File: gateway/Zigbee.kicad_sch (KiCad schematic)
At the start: 28 parts, among them IC1101 MIC5317-3.3xM5, IC1102 TXB0102DCT, IC1103 74LVC1G07, IC1104 74LVC1G07, M1101 RF-BM-2652

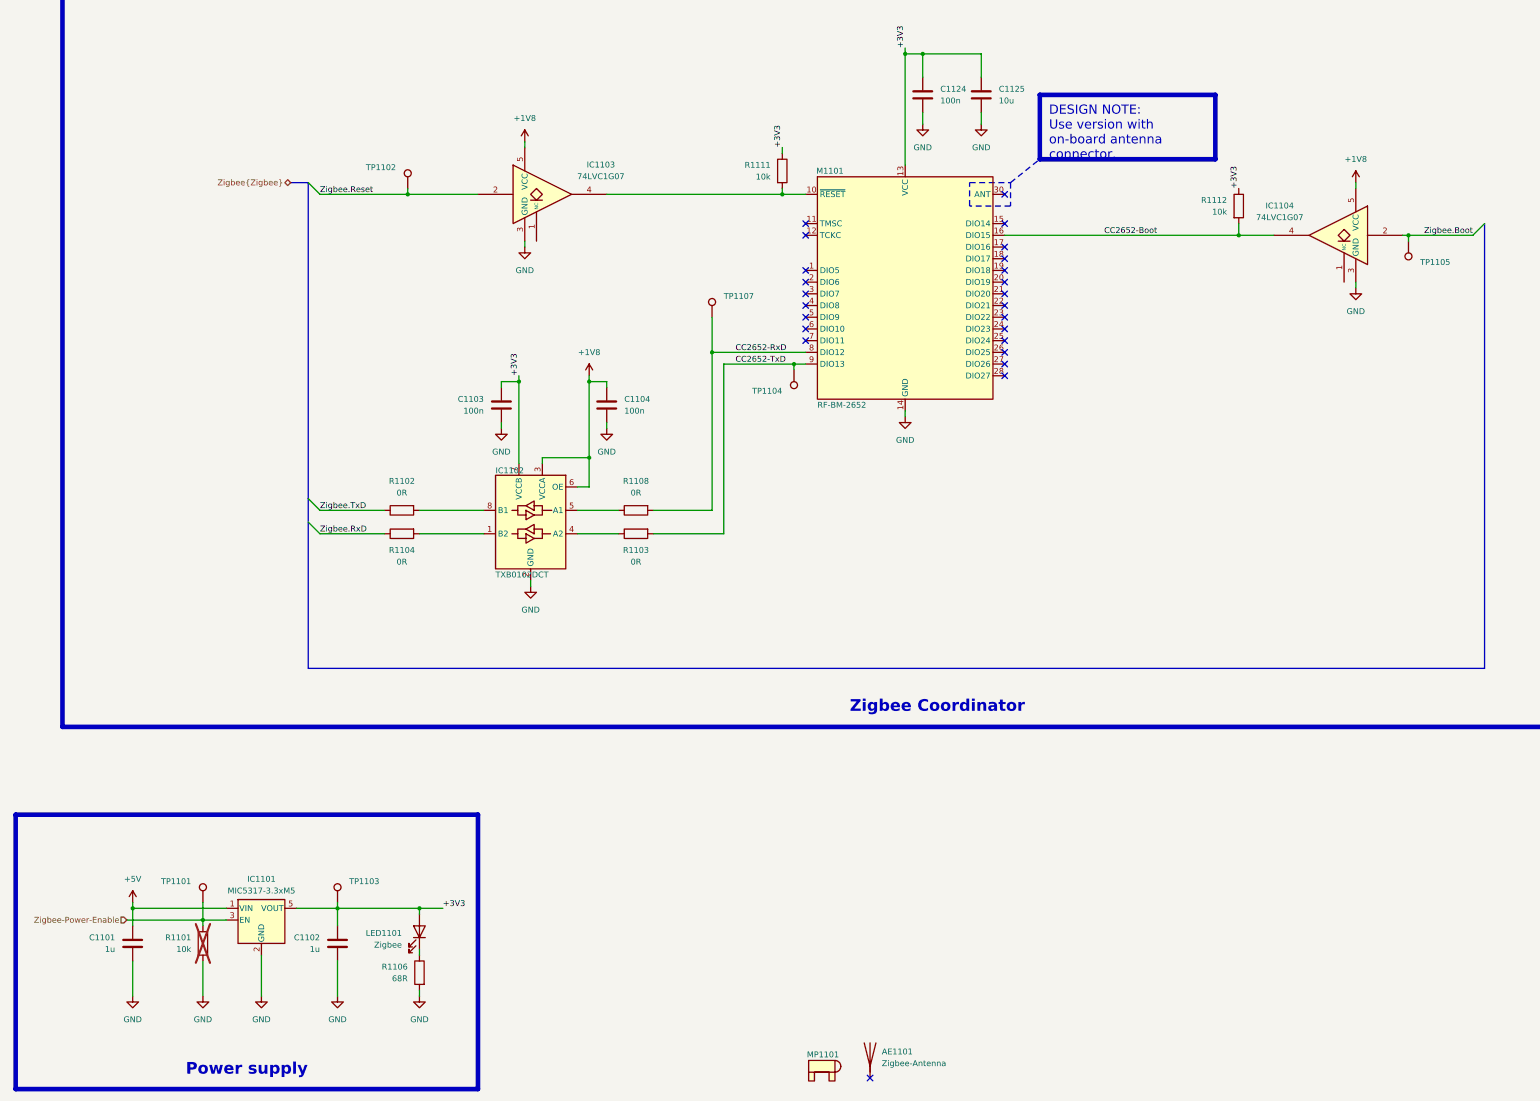
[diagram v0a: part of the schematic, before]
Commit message: Add INA219 for current measurement
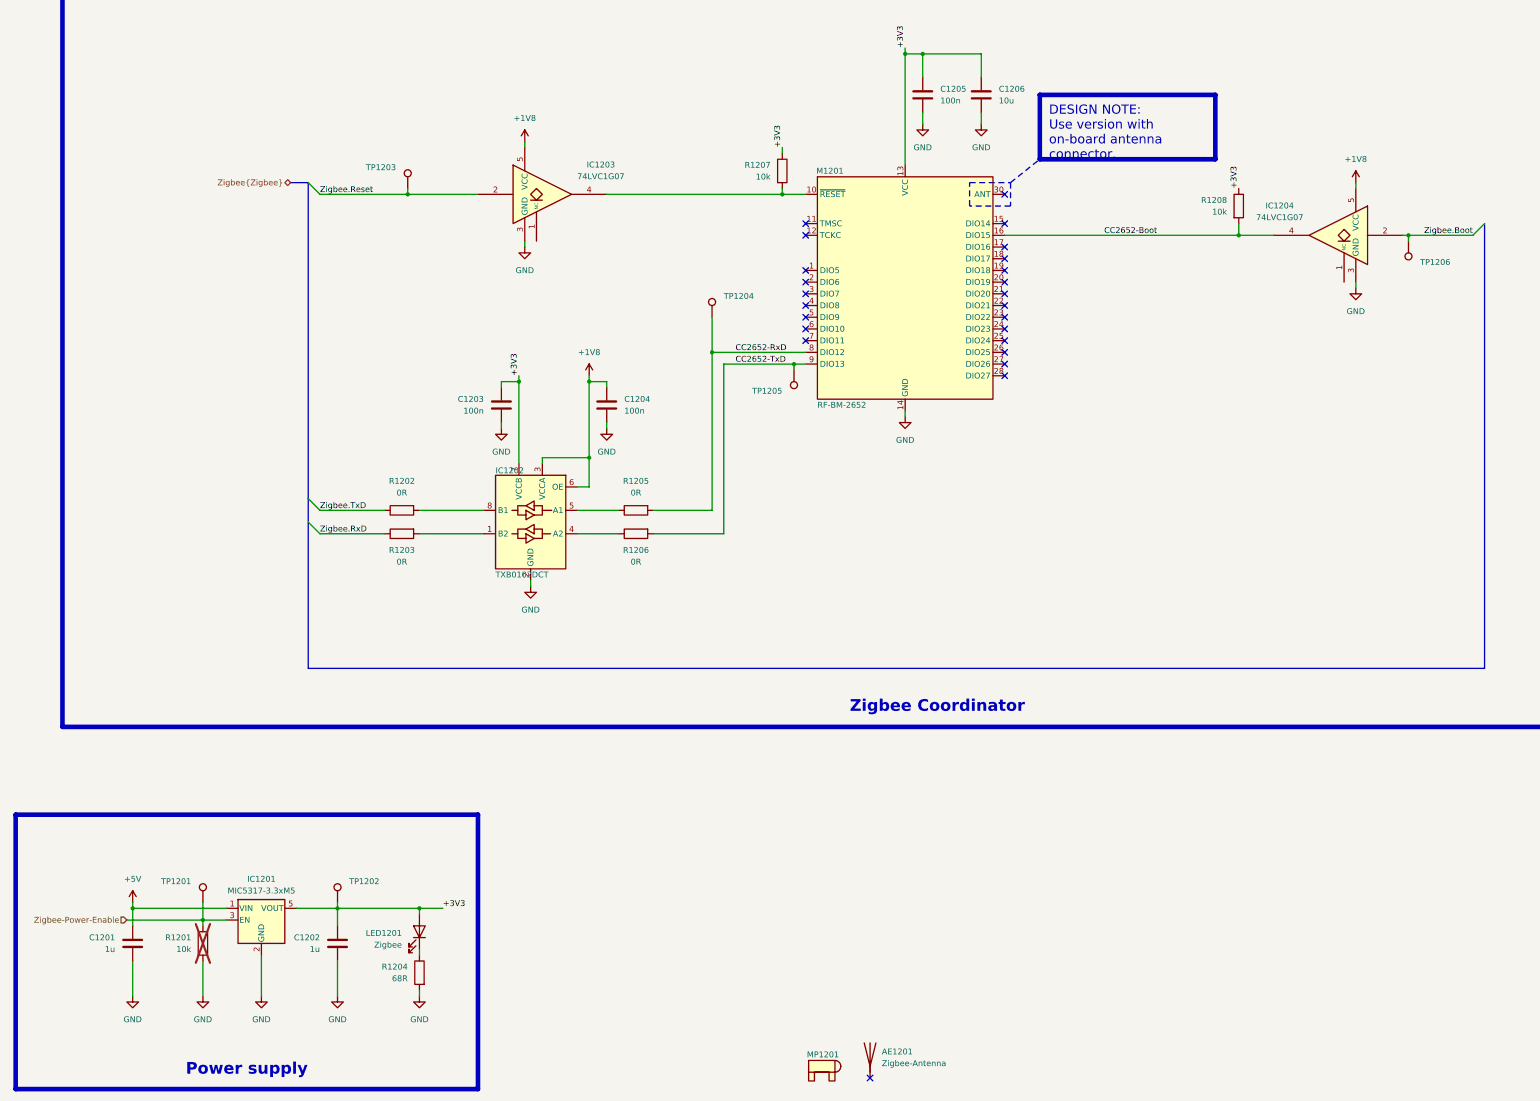
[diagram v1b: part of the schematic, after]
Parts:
- renumbered AE1101 to AE1201, C1101 to C1201, C1102 to C1202, C1103 to C1203, C1104 to C1204, C1124 to C1205, C1125 to C1206, IC1101 to IC1201, IC1102 to IC1202, IC1103 to IC1203, IC1104 to IC1204, LED1101 to LED1201, M1101 to M1201, MP1101 to MP1201, R1101 to R1201, R1102 to R1202, R1104 to R1203, R1106 to R1204, R1108 to R1205, R1103 to R1206, R1111 to R1207, R1112 to R1208, TP1101 to TP1201, TP1103 to TP1202, TP1102 to TP1203, TP1107 to TP1204, TP1104 to TP1205, TP1105 to TP1206

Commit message: Improving Thread
- Add boot signal for Thread MCU
- Add debug LED for nRF5340
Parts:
- TP1201, TP1202, TP1203, TP1204, TP1205, TP1206: value ~ -> (none)
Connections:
- net at IC1202.1 (B2): now also R1206.1; no longer R1203.2
- net at IC1202.4 (A2): now also R1203.2; no longer R1206.1
- net at IC1202.5 (A1): now also R1202.2; no longer R1205.1
- net at IC1202.8 (B1): now also R1205.1; no longer R1202.2
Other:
- moved on the sheet: C1203, C1204
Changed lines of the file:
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@@
 	)
 	(rectangle
-		(start 24.13 38.1)
-		(end 403.86 204.47)
+		(start 54.61 38.1)
+		(end 345.44 204.47)
 		(stroke
 			(width 1)
@@
 	(text_box "Zigbee Coordinator"
 		(exclude_from_sim no)
-		(at 25.4 194.31 0)
-		(size 377.19 8.89)
+		(at 55.88 194.31 0)
+		(size 288.29 8.89)
 		(margins 1.9049 1.9049 1.9049 1.9049)
 		(stroke
@@
 	)
 	(junction
-		(at 123.19 129.54)
+		(at 128.27 129.54)
 		(diameter 0)
 		(color 0 0 0 0)
@@
 	)
 	(junction
-		(at 138.43 146.05)
+		(at 113.03 146.05)
 		(diameter 0)
 		(color 0 0 0 0)
@@
 	)
 	(junction
-		(at 138.43 129.54)
+		(at 113.03 129.54)
 		(diameter 0)
 		(color 0 0 0 0)
@@
 	(wire
 		(pts
-			(xy 138.43 129.54) (xy 142.24 129.54)
+			(xy 113.03 129.54) (xy 109.22 129.54)
 		)
 		(stroke
@@
 	(wire
 		(pts
-			(xy 138.43 146.05) (xy 138.43 152.4)
+			(xy 113.03 146.05) (xy 113.03 152.4)
 		)
 		(stroke
@@
 	(wire
 		(pts
-			(xy 119.38 129.54) (xy 119.38 130.81)
+			(xy 132.08 129.54) (xy 132.08 130.81)
 		)
 		(stroke
@@
 	(wire
 		(pts
-			(xy 142.24 129.54) (xy 142.24 130.81)
+			(xy 109.22 129.54) (xy 109.22 130.81)
 		)
 		(stroke
@@
 	(wire
 		(pts
-			(xy 142.24 138.43) (xy 142.24 139.7)
+			(xy 109.22 138.43) (xy 109.22 139.7)
 		)
 		(stroke
@@
 	(wire
 		(pts
-			(xy 138.43 152.4) (xy 135.89 152.4)
+			(xy 113.03 152.4) (xy 115.57 152.4)
 		)
 		(stroke
@@
 	(wire
 		(pts
-			(xy 123.19 129.54) (xy 123.19 147.32)
+			(xy 128.27 129.54) (xy 128.27 147.32)
 		)
 		(stroke
@@
 	(wire
 		(pts
-			(xy 119.38 138.43) (xy 119.38 139.7)
+			(xy 132.08 138.43) (xy 132.08 139.7)
 		)
 		(stroke
@@
 	(wire
 		(pts
-			(xy 128.27 146.05) (xy 138.43 146.05)
+			(xy 123.19 146.05) (xy 113.03 146.05)
 		)
 		(stroke
@@
 	(wire
 		(pts
-			(xy 138.43 128.27) (xy 138.43 129.54)
+			(xy 113.03 128.27) (xy 113.03 129.54)
 		)
 		(stroke
@@
 	(wire
 		(pts
-			(xy 128.27 146.05) (xy 128.27 147.32)
+			(xy 123.19 146.05) (xy 123.19 147.32)
 		)
 		(stroke
@@
 	(wire
 		(pts
-			(xy 123.19 128.27) (xy 123.19 129.54)
+			(xy 128.27 128.27) (xy 128.27 129.54)
 		)
 		(stroke
@@
 	(wire
 		(pts
-			(xy 119.38 129.54) (xy 123.19 129.54)
+			(xy 132.08 129.54) (xy 128.27 129.54)
 		)
 		(stroke
@@
 	(wire
 		(pts
-			(xy 138.43 129.54) (xy 138.43 146.05)
+			(xy 113.03 129.54) (xy 113.03 146.05)
 		)
 		(stroke
@@
 	)
 	(label "+3V3"
-		(at 123.19 128.27 90)
+		(at 128.27 128.27 90)
 		(effects
 			(font
@@
 	(symbol
 		(lib_id "Device:C")
-		(at 119.38 134.62 0)
+		(at 132.08 134.62 0)
+		(mirror y)
 		(unit 1)
 		(body_style 1)
@@
 		(fields_autoplaced yes)
 		(property "Reference" "C1203"
-			(at 115.57 133.3499 0)
+			(at 135.89 133.3499 0)
 			(show_name no)
 			(do_not_autoplace no)
@@
 		)
 		(property "Value" "100n"
-			(at 115.57 135.8899 0)
+			(at 135.89 135.8899 0)
 			(show_name no)
 			(do_not_autoplace no)
@@
 		)
 		(property "Footprint" "Capacitor_SMD:C_0805_2012Metric"
-			(at 120.3452 138.43 0)
+			(at 131.1148 138.43 0)
 			(hide yes)
 			(show_name no)
@@
 		)
 		(property "Datasheet" "https://datasheets.kyocera-avx.com/AutoMLCC.pdf"
-			(at 119.38 134.62 0)
+			(at 132.08 134.62 0)
 			(hide yes)
 			(show_name no)
@@
 		)
 		(property "Description" "Unpolarized capacitor"
-			(at 119.38 134.62 0)
+			(at 132.08 134.62 0)
 			(hide yes)
 			(show_name no)
@@
 		)
 		(property "manf" "KYOCERA AVX"
-			(at 119.38 134.62 0)
+			(at 132.08 134.62 0)
 			(hide yes)
 			(show_name no)
@@
 		)
 		(property "manf#" "08053C104M4T4A"
-			(at 119.38 134.62 0)
+			(at 132.08 134.62 0)
 			(hide yes)
 			(show_name no)
@@
 		)
 		(property "mouser#" "581-08053C104M4T4A"
-			(at 119.38 134.62 0)
+			(at 132.08 134.62 0)
 			(hide yes)
 			(show_name no)
@@
 		(lib_id "Logic_LevelTranslator:TXB0102DCT")
 		(at 125.73 160.02 0)
-		(mirror y)
 		(unit 1)
 		(body_style 1)
@@
 		(dnp no)
 		(property "Reference" "IC1202"
-			(at 118.11 148.844 0)
+			(at 133.35 148.844 0)
 			(show_name no)
 			(do_not_autoplace no)
@@
 		)
 		(property "Value" "TXB0102DCT"
-			(at 118.11 171.45 0)
+			(at 133.35 171.45 0)
 			(show_name no)
 			(do_not_autoplace no)
@@
 			)
 		)
-		(property "Value" "~"
+		(property "Value" ""
 			(at 167.64 113.5379 0)
 			(show_name no)
@@
 	(symbol
 		(lib_id "Device:C")
-		(at 142.24 134.62 0)
-		(mirror y)
+		(at 109.22 134.62 0)
 		(unit 1)
 		(body_style 1)
@@
 		(dnp no)
 		(property "Reference" "C1204"
-			(at 146.05 133.3499 0)
+			(at 105.41 133.3499 0)
 			(show_name no)
 			(do_not_autoplace no)
@@
 		)
 		(property "Value" "100n"
-			(at 146.05 135.8899 0)
+			(at 105.41 135.8899 0)
 			(show_name no)
 			(do_not_autoplace no)
@@
 		)
 		(property "Footprint" "Capacitor_SMD:C_0805_2012Metric"
-			(at 141.2748 138.43 0)
+			(at 110.1852 138.43 0)
 			(hide yes)
 			(show_name no)
@@
 		)
 		(property "Datasheet" "https://datasheets.kyocera-avx.com/AutoMLCC.pdf"
-			(at 142.24 134.62 0)
+			(at 109.22 134.62 0)
 			(hide yes)
 			(show_name no)
@@
 		)
 		(property "Description" "Unpolarized capacitor"
-			(at 142.24 134.62 0)
+			(at 109.22 134.62 0)
 			(hide yes)
 			(show_name no)
@@
 		)
 		(property "manf" "KYOCERA AVX"
-			(at 142.24 134.62 0)
+			(at 109.22 134.62 0)
 			(hide yes)
 			(show_name no)
@@
 		)
 		(property "manf#" "08053C104M4T4A"
-			(at 142.24 134.62 0)
+			(at 109.22 134.62 0)
 			(hide yes)
 			(show_name no)
@@
 		)
 		(property "mouser#" "581-08053C104M4T4A"
-			(at 142.24 134.62 0)
+			(at 109.22 134.62 0)
 			(hide yes)
 			(show_name no)
@@
 			)
 		)
-		(property "Value" "~"
+		(property "Value" ""
 			(at 86.36 240.5379 0)
 			(show_name no)
@@
 	(symbol
 		(lib_id "power:GND")
-		(at 119.38 139.7 0)
-		(mirror y)
+		(at 132.08 139.7 0)
 		(unit 1)
 		(body_style 1)
@@
 		(fields_autoplaced yes)
 		(property "Reference" "#PWR01207"
-			(at 119.38 146.05 0)
+			(at 132.08 146.05 0)
 			(hide yes)
 			(show_name no)
@@
 		)
 		(property "Value" "GND"
-			(at 119.38 144.78 0)
+			(at 132.08 144.78 0)
 			(show_name no)
 			(do_not_autoplace no)
@@
 		)
 		(property "Footprint" ""
-			(at 119.38 139.7 0)
+			(at 132.08 139.7 0)
 			(hide yes)
 			(show_name no)
@@
 		)
 		(property "Datasheet" ""
-			(at 119.38 139.7 0)
+			(at 132.08 139.7 0)
 			(hide yes)
 			(show_name no)
@@
 		)
 		(property "Description" "Power symbol creates a global label with name \"GND\" , ground"
-			(at 119.38 139.7 0)
+			(at 132.08 139.7 0)
 			(hide yes)
 			(show_name no)
@@
 			)
 		)
-		(property "Value" "~"
+		(property "Value" ""
 			(at 52.07 240.5379 0)
 			(show_name no)
@@
 		(lib_id "power:GND")
 		(at 125.73 173.99 0)
+		(mirror y)
 		(unit 1)
 		(body_style 1)
@@
 			)
 		)
-		(property "Value" "~"
+		(property "Value" ""
 			(at 96.52 85.5979 0)
 			(show_name no)
@@
 	(symbol
 		(lib_id "power:GND")
-		(at 142.24 139.7 0)
+		(at 109.22 139.7 0)
+		(mirror y)
 		(unit 1)
 		(body_style 1)
@@
 		(fields_autoplaced yes)
 		(property "Reference" "#PWR01212"
-			(at 142.24 146.05 0)
+			(at 109.22 146.05 0)
 			(hide yes)
 			(show_name no)
@@
 		)
 		(property "Value" "GND"
-			(at 142.24 144.78 0)
+			(at 109.22 144.78 0)
 			(show_name no)
 			(do_not_autoplace no)
@@
 		)
 		(property "Footprint" ""
-			(at 142.24 139.7 0)
+			(at 109.22 139.7 0)
 			(hide yes)
 			(show_name no)
@@
 		)
 		(property "Datasheet" ""
-			(at 142.24 139.7 0)
+			(at 109.22 139.7 0)
 			(hide yes)
 			(show_name no)
@@
 		)
 		(property "Description" "Power symbol creates a global label with name \"GND\" , ground"
-			(at 142.24 139.7 0)
+			(at 109.22 139.7 0)
 			(hide yes)
 			(show_name no)
@@
 			)
 		)
-		(property "Value" "~"
+		(property "Value" ""
 			(at 318.77 101.0921 0)
 			(show_name no)
@@
 			)
 		)
-		(property "Value" "~"
+		(property "Value" ""
 			(at 180.34 129.0321 0)
 			(show_name no)
@@
 	(symbol
 		(lib_id "power:+1V8")
-		(at 138.43 128.27 0)
+		(at 113.03 128.27 0)
+		(mirror y)
 		(unit 1)
 		(body_style 1)
@@
 		(fields_autoplaced yes)
 		(property "Reference" "#PWR01211"
-			(at 138.43 132.08 0)
+			(at 113.03 132.08 0)
 			(hide yes)
 			(show_name no)
@@
 		)
 		(property "Value" "+1V8"
-			(at 138.43 123.19 0)
+			(at 113.03 123.19 0)
 			(show_name no)
 			(do_not_autoplace no)
@@
 		)
 		(property "Footprint" ""
-			(at 138.43 128.27 0)
+			(at 113.03 128.27 0)
 			(hide yes)
 			(show_name no)
@@
 		)
 		(property "Datasheet" ""
-			(at 138.43 128.27 0)
+			(at 113.03 128.27 0)
 			(hide yes)
 			(show_name no)
@@
 		)
 		(property "Description" "Power symbol creates a global label with name \"+1V8\""
-			(at 138.43 128.27 0)
+			(at 113.03 128.27 0)
 			(hide yes)
 			(show_name no)
